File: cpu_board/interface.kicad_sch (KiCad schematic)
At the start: 8 parts

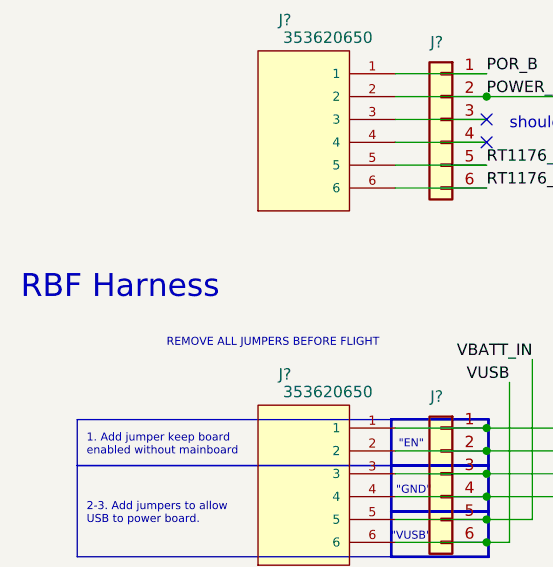
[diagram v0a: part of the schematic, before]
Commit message: clean up board2board connector and organize TODOs
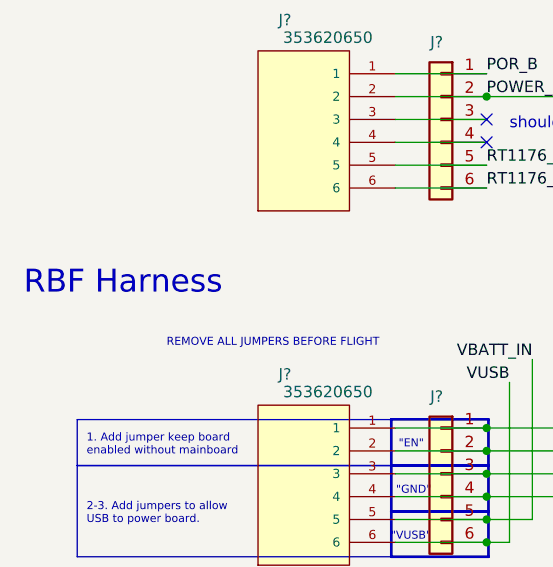
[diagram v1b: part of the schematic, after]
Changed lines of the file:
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@@
     (effects (font (size 0.889 0.889)) (justify left bottom))
   )
-  (text "RBF Harness" (at 157.1498 140.1826 0)
+  (text "RBF Harness" (at 157.48 139.7 0)
     (effects (font (size 2.54 2.54)) (justify left bottom))
   )

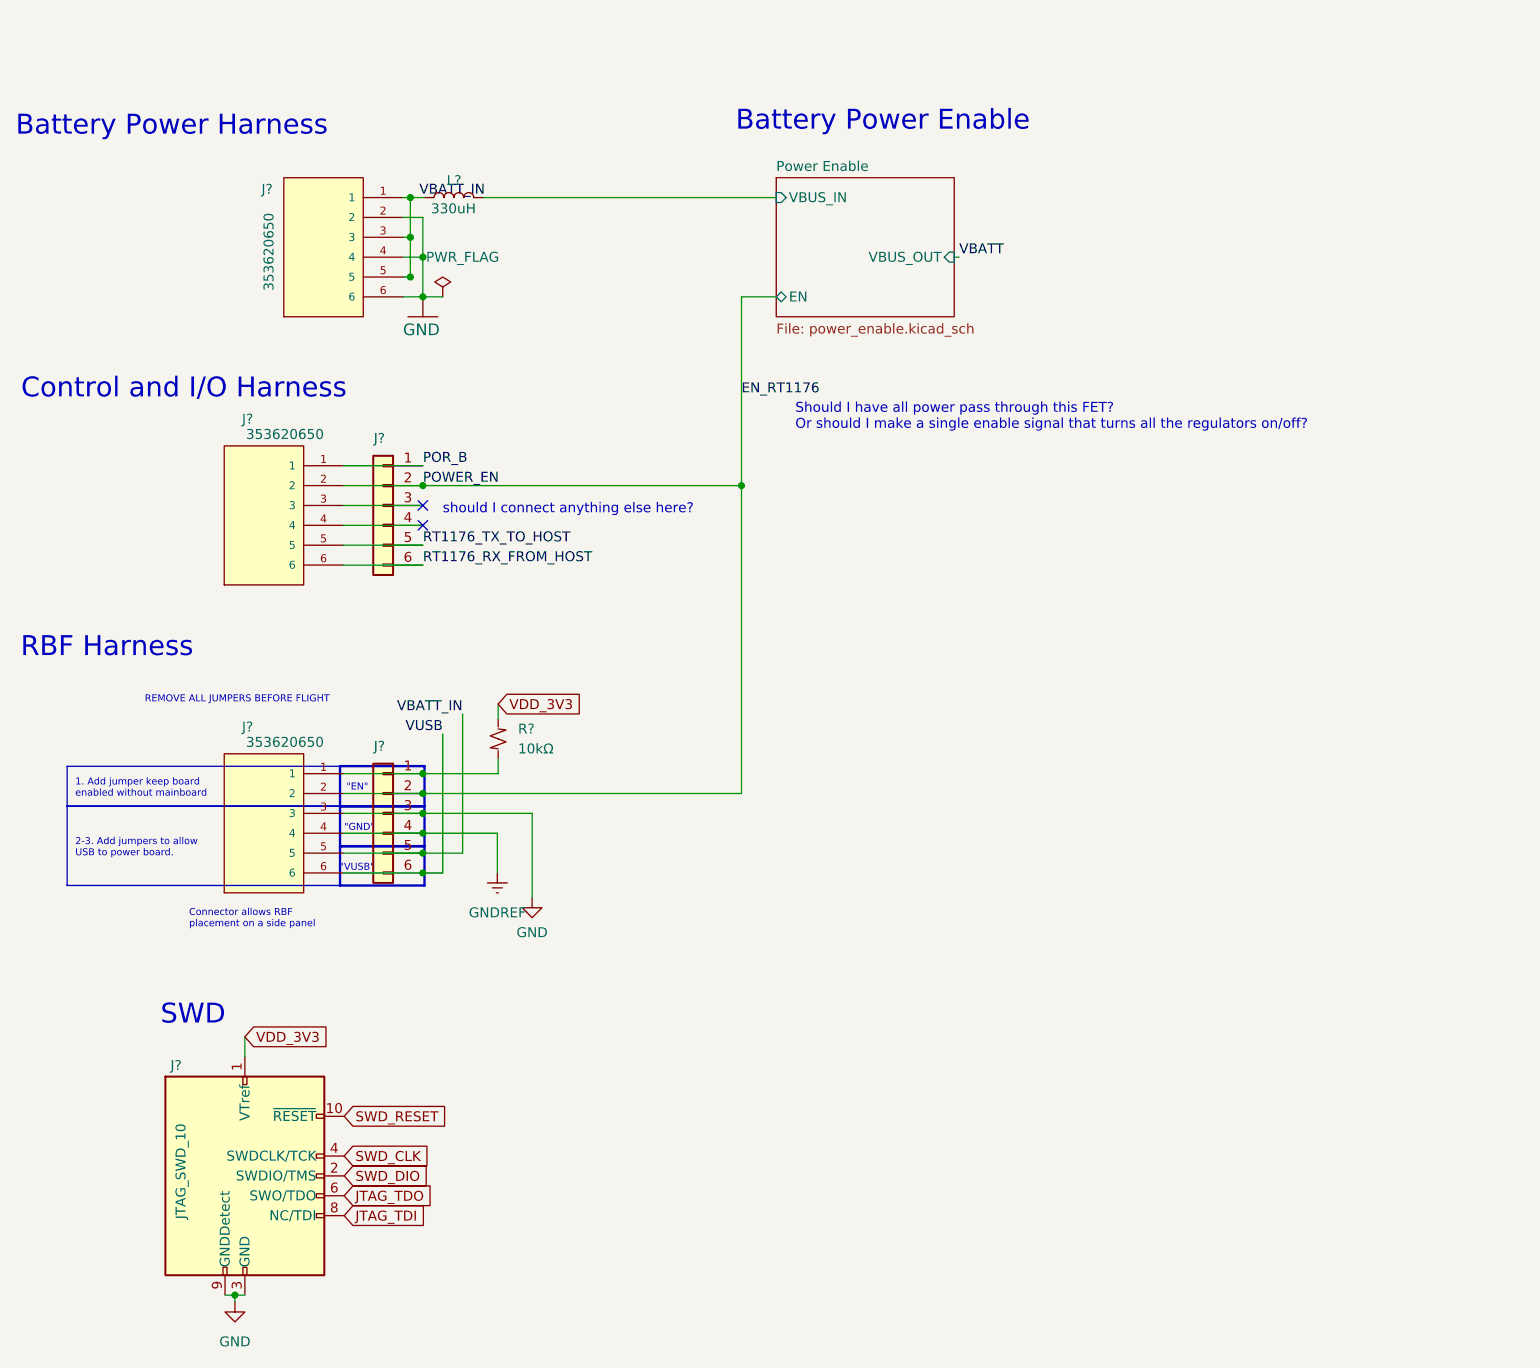
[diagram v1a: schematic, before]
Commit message: route most of power distribution
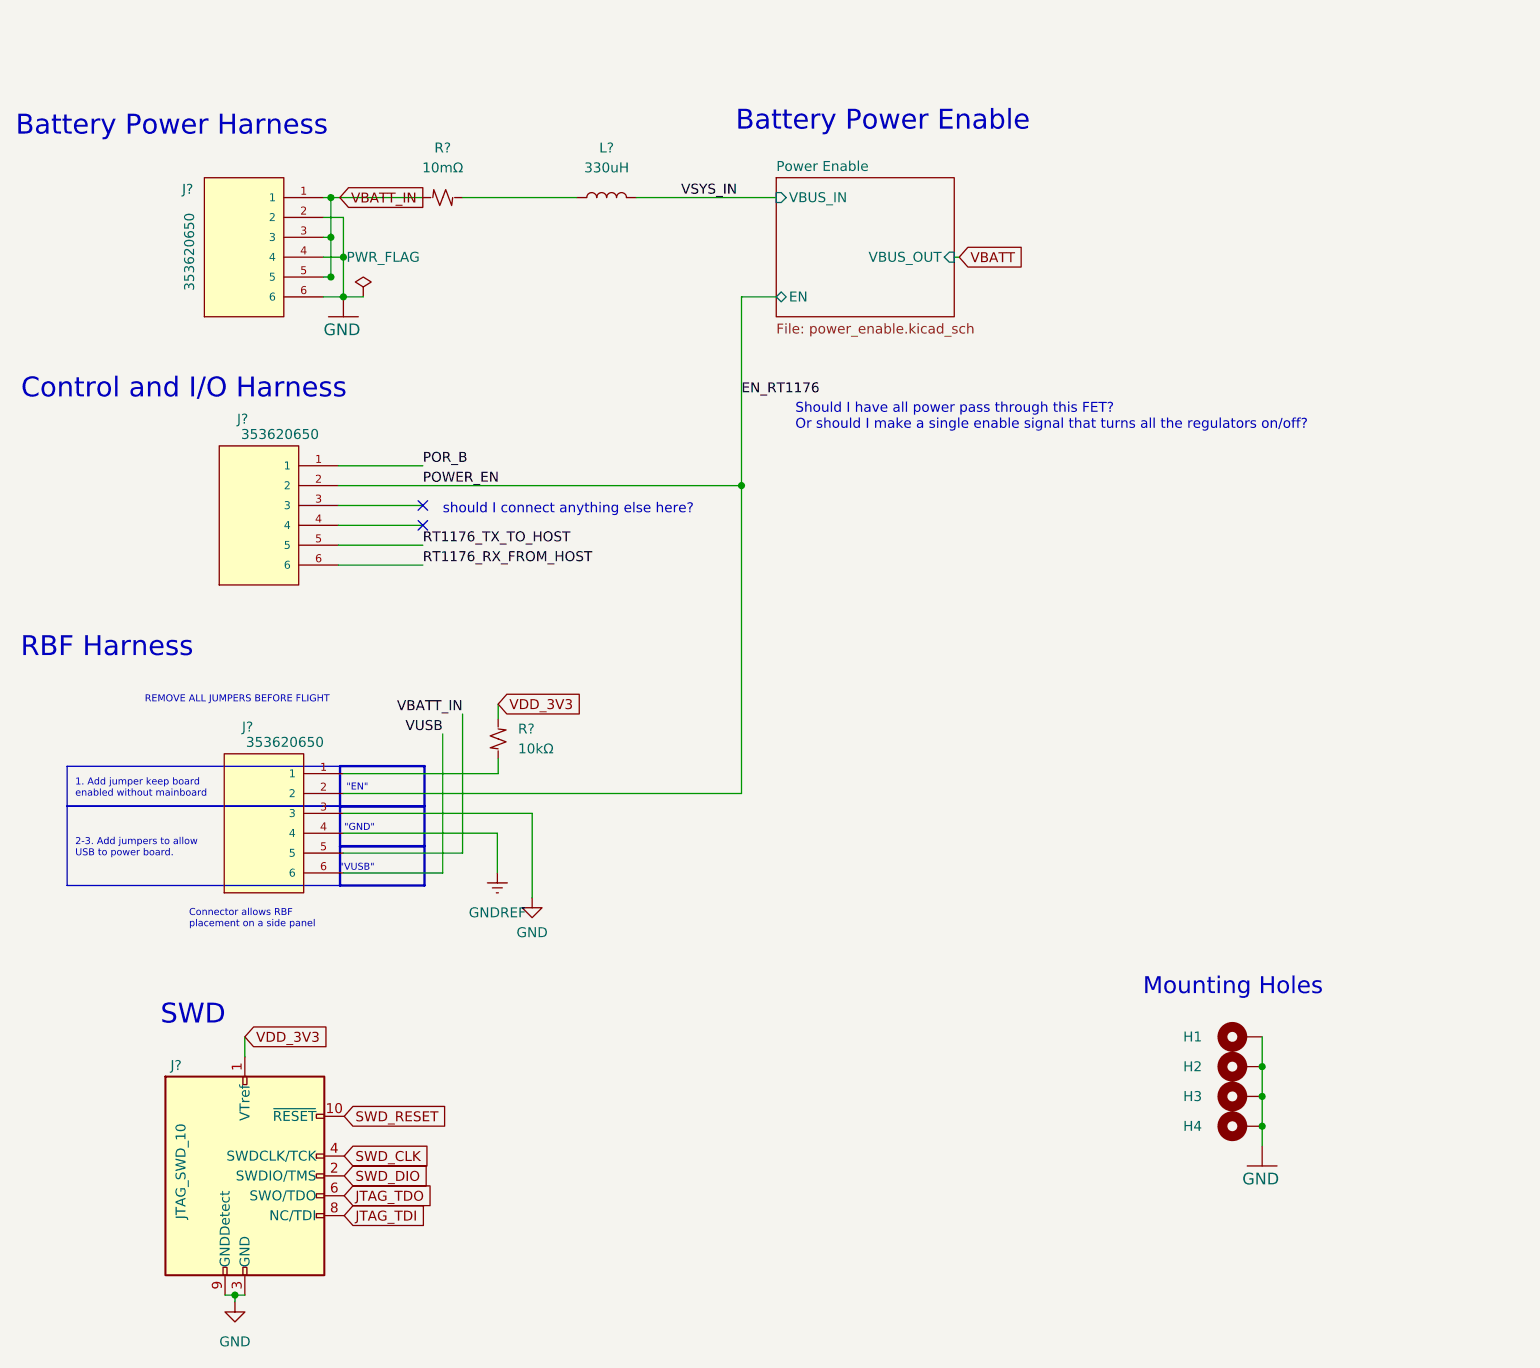
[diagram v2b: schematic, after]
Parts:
- removed J? (x2): Conn_01x06, Connector_PinHeader_2.54mm:PinHeader_1x06_P2.54mm_Vertical, symbol Connector_Generic:Conn_01x06
- removed L?: 330uH, adcs:IND_SRN6045TA-331K, symbol Device:L
- added H1, H2, H3, H4: MountingHole_Pad, MountingHole:MountingHole_2.7mm_M2.5_DIN965_Pad, symbol Mechanical:MountingHole_Pad
- added L?: 330uH, adcs:IND_SRN6045TA-331K, symbol Device:L
- added R?: 10mΩ, Resistor_SMD:R_2512_6332Metric, symbol Device:R_Small_US
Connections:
- net GND: now also H1.1, H2.1, H3.1, H4.1
- net VBATT_IN: now also R?.1
- new net: L?.1, R?.2
- new net VSYS_IN: L?.2
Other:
- note added: "Mounting Holes"
- moved on the sheet: J?

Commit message: floorplan complete
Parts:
- removed J?: 353620650, mainboard:MOLEX_35362-0650, symbol mainboard:35362-0650
- added J5: Conn_01x06, Connector_PinHeader_2.54mm:PinHeader_1x06_P2.54mm_Vertical, symbol Connector_Generic:Conn_01x06
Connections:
- net EN_RT1176: now also J5.2 (Pin_2)
- net GND: now also J5.3 (Pin_3)
- net GNDREF: now also J5.4 (Pin_4)
- net VBATT_IN: now also J5.5 (Pin_5)
- net VUSB: now also J5.6 (Pin_6)
- net at R?.2: now also J5.1 (Pin_1)

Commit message: continue work on fanout
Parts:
- R?: footprint Resistor_SMD:R_0402_1005Metric -> adcs:Perfect_0402
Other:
- note added: "Could add power monitoring circuitry here"
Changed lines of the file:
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@@
     (effects (font (size 1.27 1.27) (color 194 0 0 1)) (justify left bottom))
+  )
+  (text "Could add power monitoring circuitry here" (at 193.04 59.69 0)
+    (effects (font (size 1.27 1.27)) (justify left bottom))
   )
   (text "Connector allows RBF\nplacement on a side panel\n" (at 179.0192 174.1678 0)
@@
       (effects (font (size 1.27 1.27)) (justify left))
     )
-    (property "Footprint" "Resistor_SMD:R_0402_1005Metric" (at 218.5416 149.86 0)
-      (effects (font (size 1.27 1.27)) hide)
-    )
+    (property "Footprint" "adcs:Perfect_0402" (at 218.5416 149.86 0)
+      (effects (font (size 1.27 1.27)) hide)
+    )

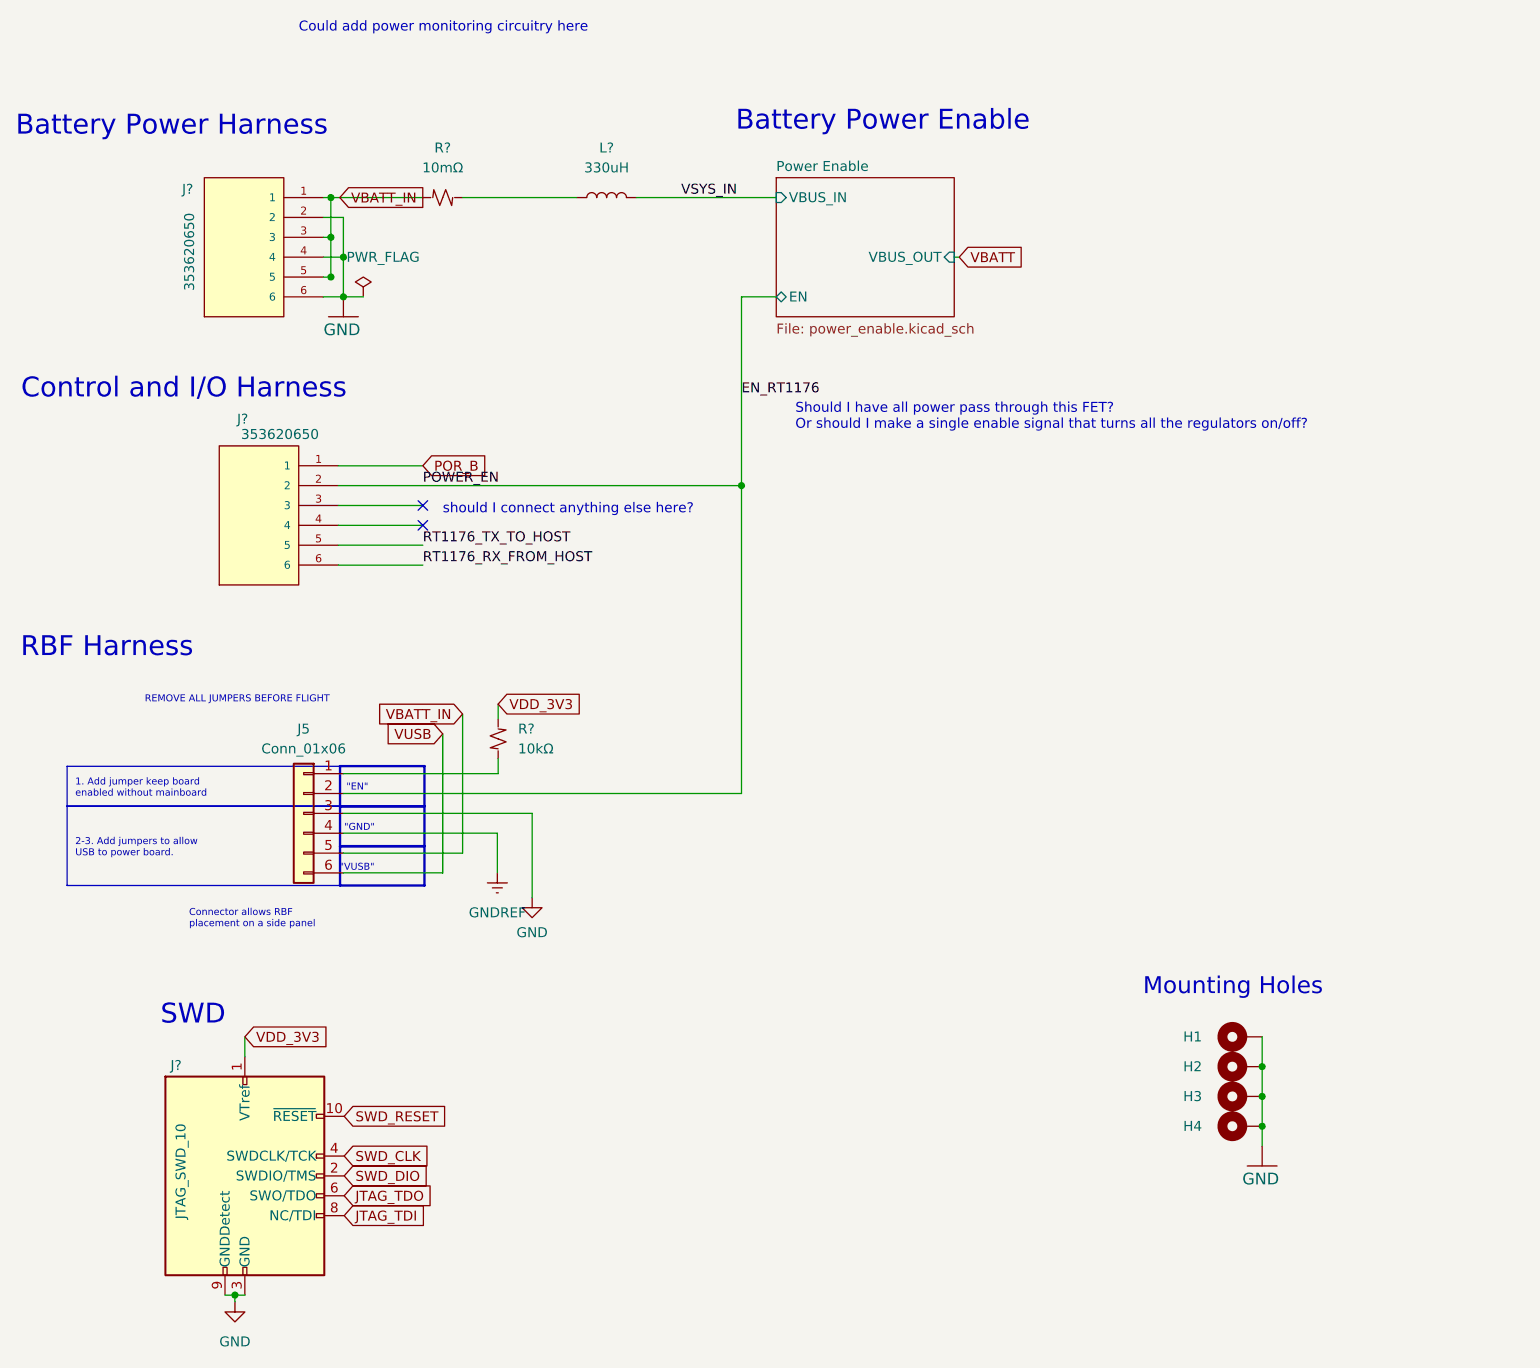
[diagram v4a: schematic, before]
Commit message: add load switch
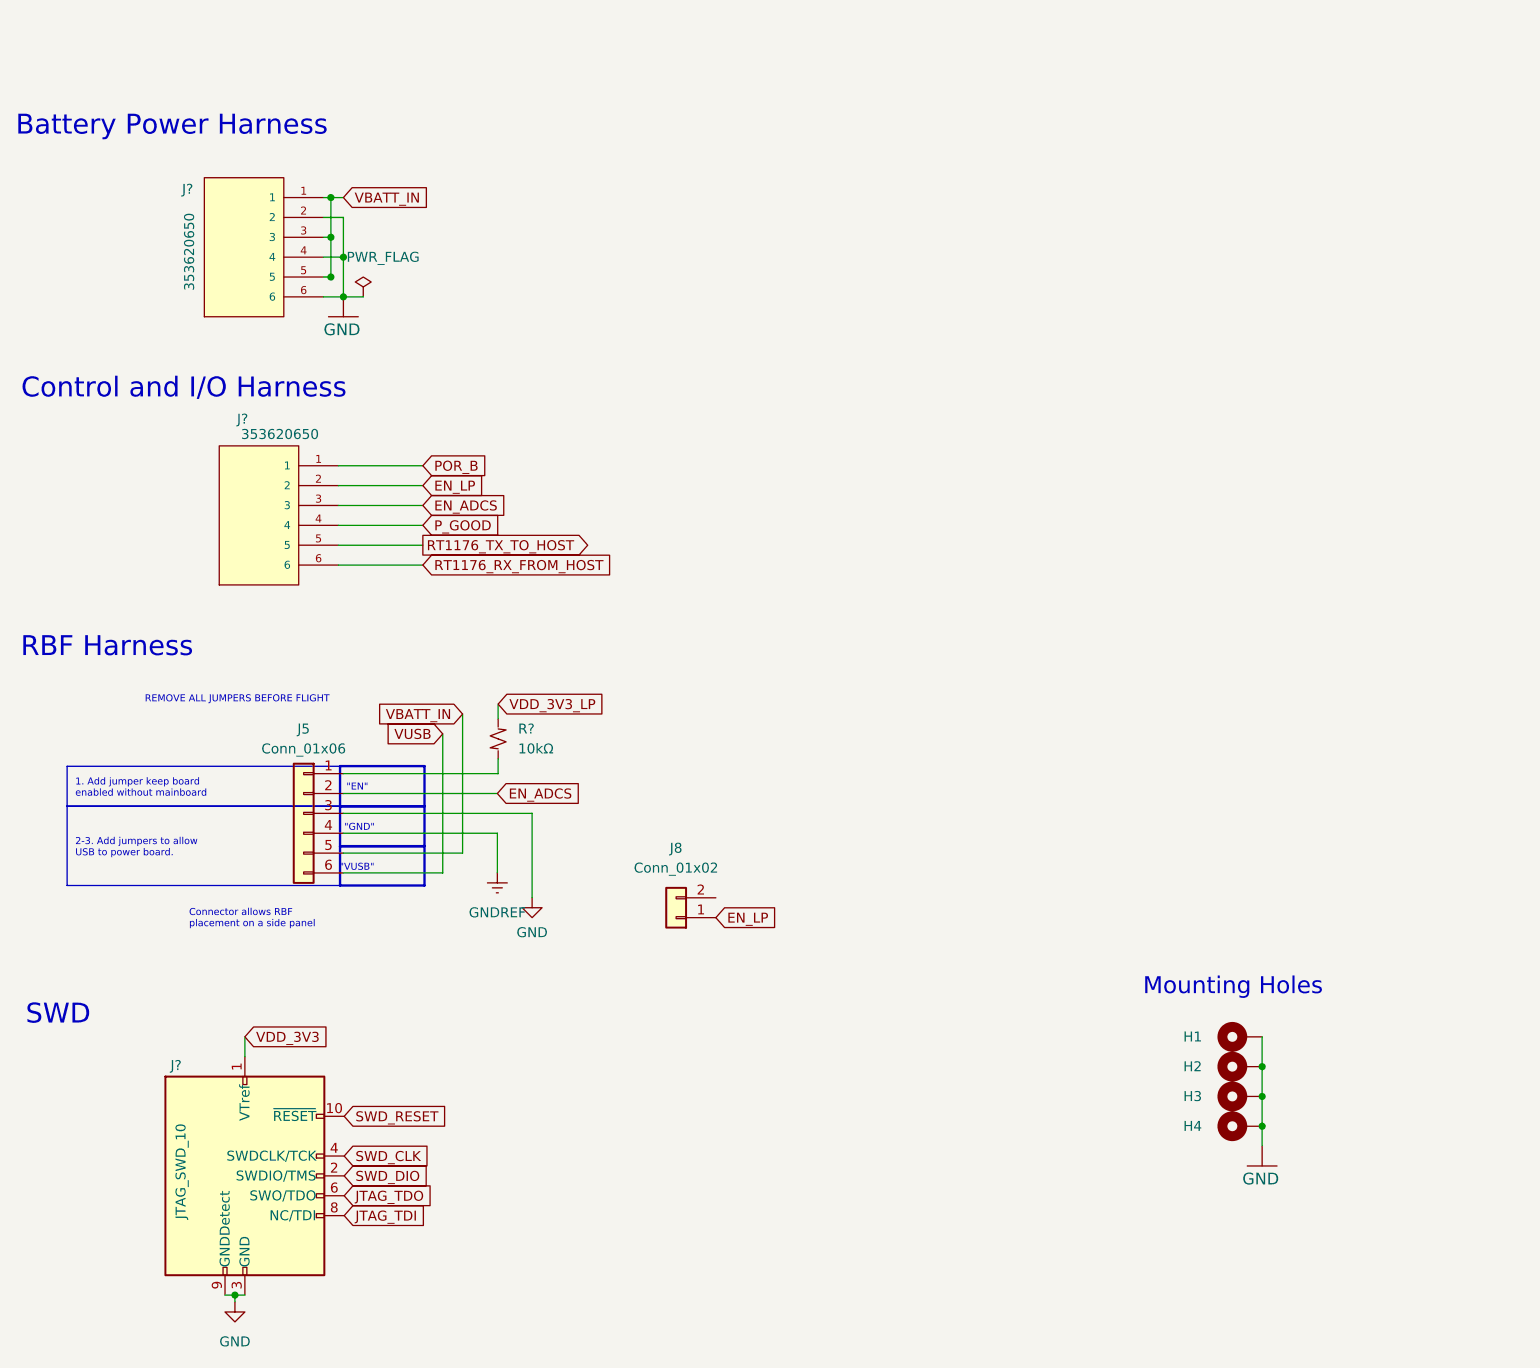
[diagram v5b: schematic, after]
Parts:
- removed L?: 330uH, adcs:IND_SRN6045TA-331K, symbol Device:L
- removed R?: 10mΩ, Resistor_SMD:R_2512_6332Metric, symbol Device:R_Small_US
- added J8: Conn_01x02, symbol Connector_Generic:Conn_01x02
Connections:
- net VDD_3V3: no longer R?.1
- net EN_ADCS: now reaches J?.3
- net EN_ADCS: now also J5.2 (Pin_2)
- net P_GOOD: now reaches J?.4
- net EN_RT1176 renamed EN_LP
- net EN_LP: now also J8.1 (Pin_1); no longer J5.2 (Pin_2)
- new net VDD_3V3_LP: R?.1
- no-connect marks 2 -> 0
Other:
- removed sheet Power Enable
- note removed: "Battery Power Enable"
- note removed: "Could add power monitoring circuitry here"
- note removed: "Should I have all power pass through this FET? Or should I make a single enable signal that turns all the regulators on/off?"
- note removed: "should I connect anything else here?"
